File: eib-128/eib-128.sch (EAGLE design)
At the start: 46 parts

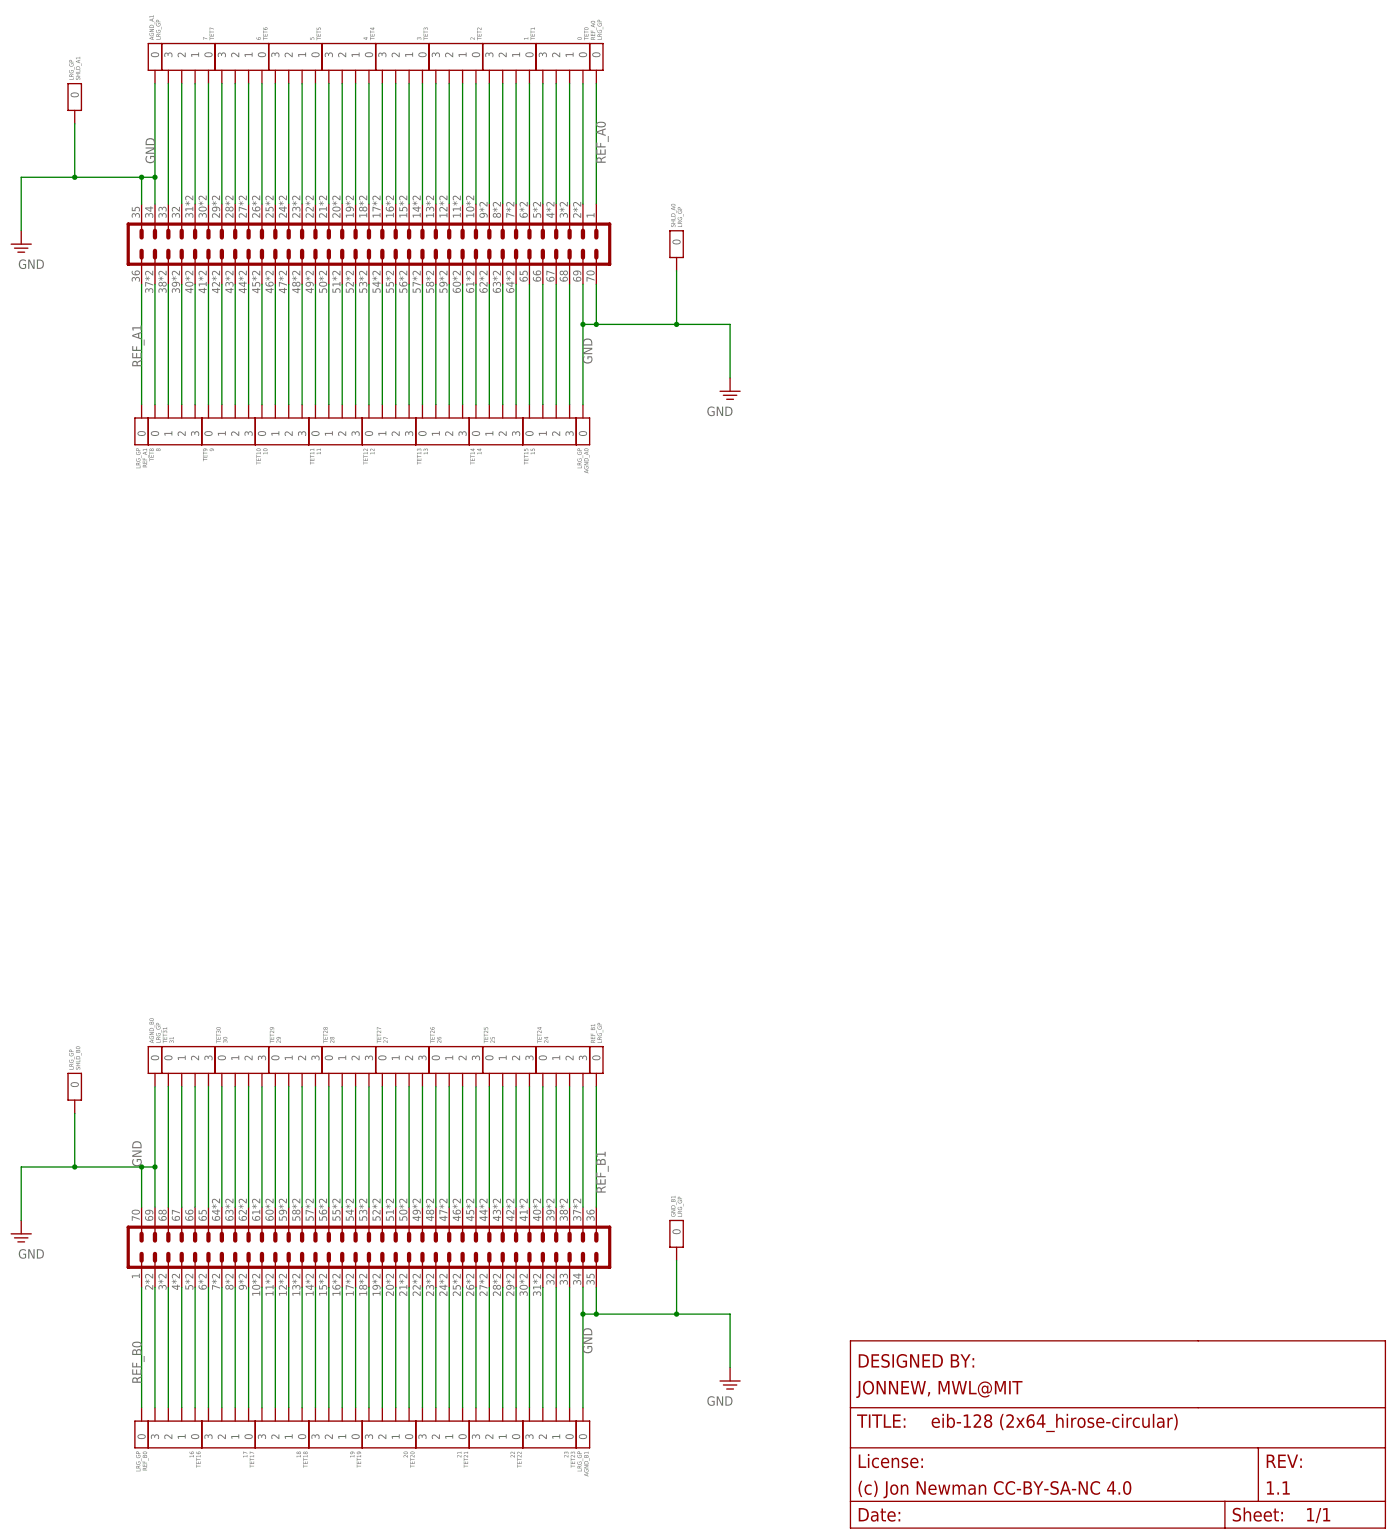
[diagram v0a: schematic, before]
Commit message: Updated eib-128 to match next-gen drive form factor.
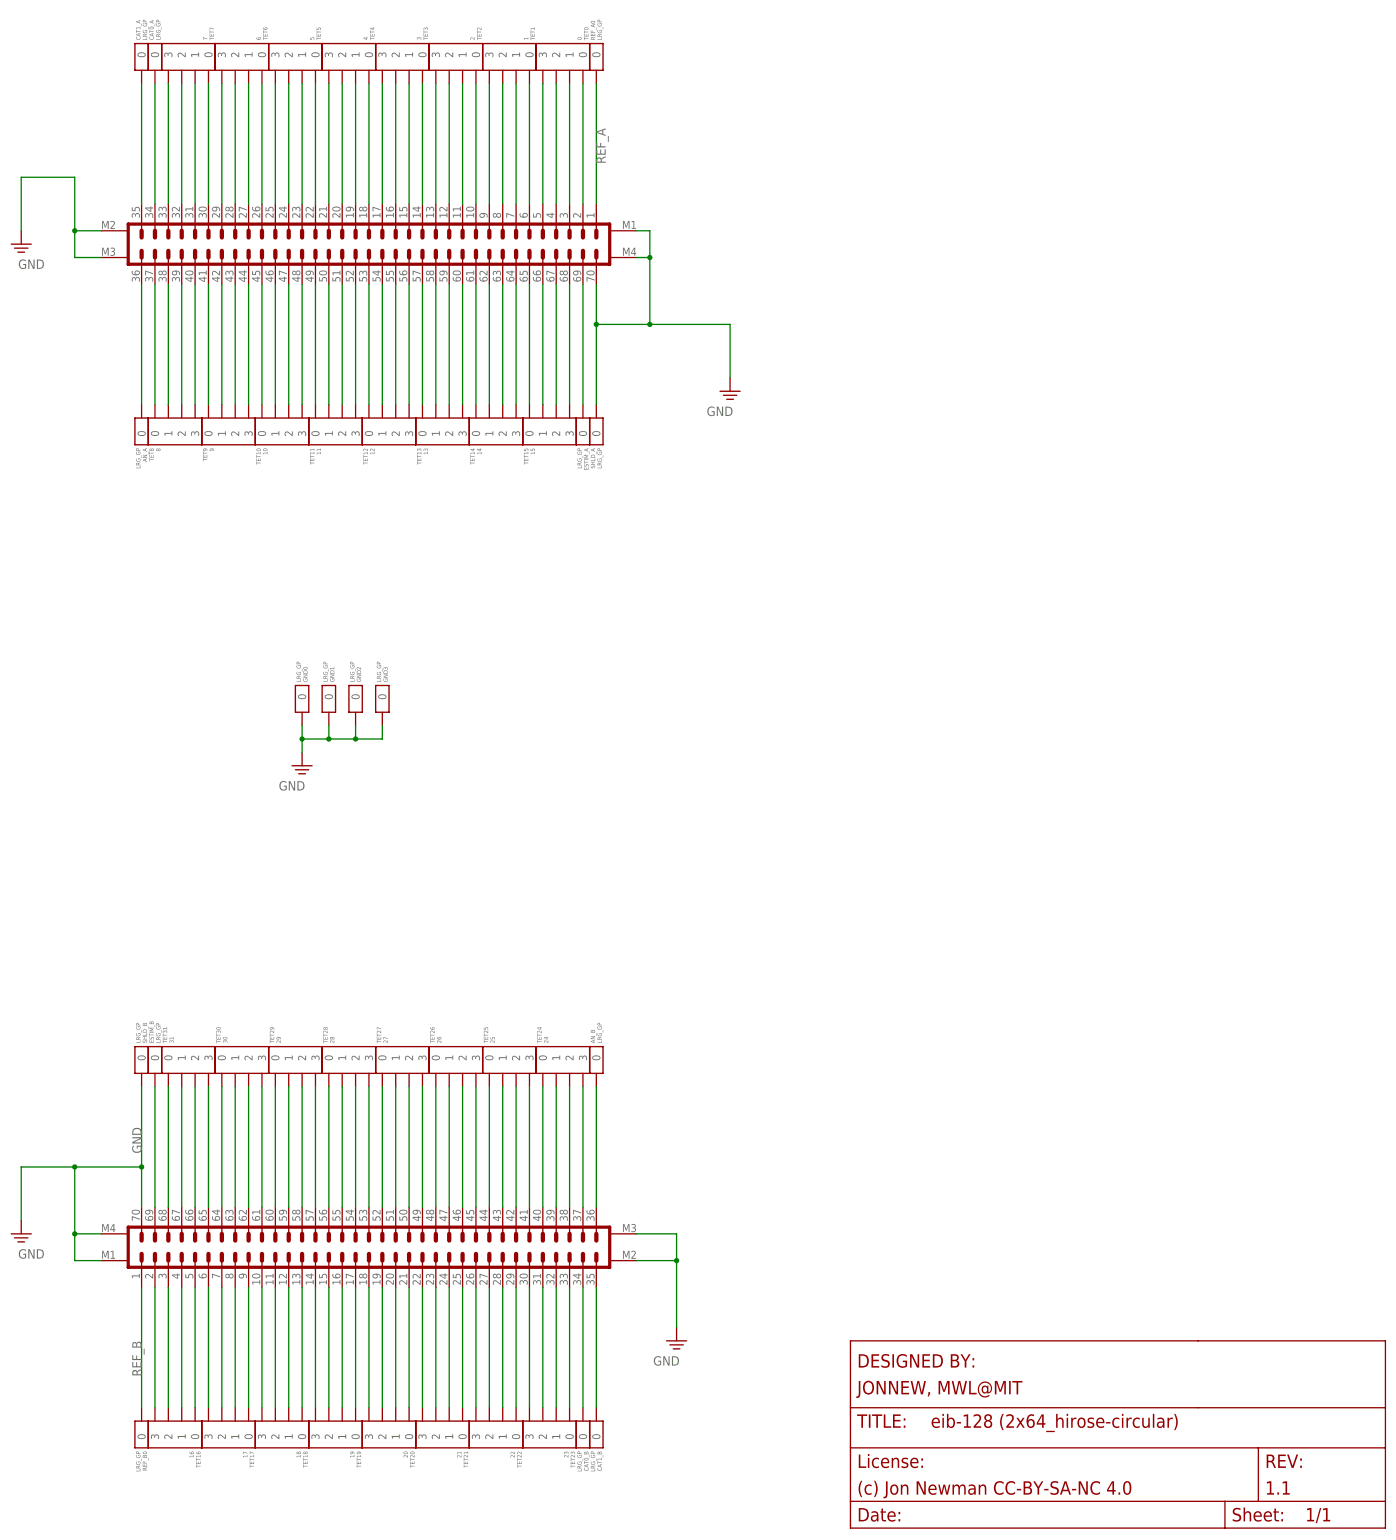
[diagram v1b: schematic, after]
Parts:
- removed AIN_N0T, AIN_S0T: DF40HEAD, jonnew:PINHD-2X35_DF40HEAD-EIB
- removed GND_B1, SHLD_A0, SHLD_A1, SHLD_B0: LRG_GP, jonnew:GOLDPIN_0.5ID_0.7OD
- added A, B: DF40HEAD, jonnew:PINHD-2X35+4_DF40-70HEAD
- added CAT1_A, CAT1_B, GND0, GND1, GND2, GND3, SHLD_A, SHLD_B: LRG_GP, jonnew:GOLDPIN_0.5ID_0.7OD
- renumbered AGND_A0 to ESTIM_A, AGND_A1 to CAT0_A, AGND_B0 to ESTIM_B, AGND_B1 to CAT0_B, REF_A1 to AN_A, REF_B1 to AN_B
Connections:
- removed net REF_A0: AIN_N0T.1, REF_A0.0
- removed net REF_A1: AIN_N0T.36, AN_A.0
- removed net REF_B0: AIN_S0T.1, REF_B0.0
- removed net REF_B1: AIN_S0T.36, AN_B.0
- new net AN_A: A.36, AN_A.0
- new net AN_B: AN_B.0, B.36
- new net CAT0_A: A.34, CAT0_A.0
- new net CAT0_B: B.34, CAT0_B.0
- new net CAT1_A: A.35, CAT1_A.0
- new net CAT1_B: B.35, CAT1_B.0
- new net ESTIM_A: A.69, ESTIM_A.0
- new net ESTIM_B: B.69, ESTIM_B.0
- new net REF_A: A.1, REF_A0.0
- new net REF_B: B.1, REF_B0.0
- net GND: now also A.70, A.M1, A.M2, A.M3, A.M4, B.70, B.M1, B.M2, B.M3, B.M4, GND0.0, GND1.0, GND2.0, GND3.0, SHLD_A.0, SHLD_B.0; no longer AIN_N0T.34, AIN_N0T.35, AIN_N0T.69, AIN_N0T.70, AIN_S0T.34, AIN_S0T.35, AIN_S0T.69, AIN_S0T.70, CAT0_A.0, CAT0_B.0, ESTIM_A.0, ESTIM_B.0, GND_B1.0, SHLD_A0.0, SHLD_A1.0, SHLD_B0.0
- net N$100: now also B.42; no longer AIN_S0T.42
- net N$1000: now also A.37; no longer AIN_N0T.37
- net N$101: now also B.43; no longer AIN_S0T.43
- net N$102: now also B.44; no longer AIN_S0T.44
- net N$103: now also B.45; no longer AIN_S0T.45
- net N$104: now also B.46; no longer AIN_S0T.46
- net N$105: now also B.47; no longer AIN_S0T.47
- net N$106: now also B.48; no longer AIN_S0T.48
- net N$107: now also B.49; no longer AIN_S0T.49
- net N$108: now also B.50; no longer AIN_S0T.50
- net N$109: now also B.51; no longer AIN_S0T.51
- net N$110: now also B.52; no longer AIN_S0T.52
- net N$111: now also B.53; no longer AIN_S0T.53
- net N$112: now also B.54; no longer AIN_S0T.54
- net N$113: now also B.55; no longer AIN_S0T.55
- net N$114: now also B.56; no longer AIN_S0T.56
- net N$115: now also B.57; no longer AIN_S0T.57
- net N$116: now also B.58; no longer AIN_S0T.58
- net N$117: now also B.59; no longer AIN_S0T.59
- net N$118: now also B.60; no longer AIN_S0T.60
- net N$119: now also B.61; no longer AIN_S0T.61
- net N$120: now also B.62; no longer AIN_S0T.62
- net N$121: now also B.63; no longer AIN_S0T.63
- net N$122: now also B.64; no longer AIN_S0T.64
- net N$123: now also B.65; no longer AIN_S0T.65
- net N$124: now also B.66; no longer AIN_S0T.66
- net N$125: now also B.67; no longer AIN_S0T.67
- net N$126: now also B.68; no longer AIN_S0T.68
- net N$127: now also B.2; no longer AIN_S0T.2
- net N$128: now also B.37; no longer AIN_S0T.37
- net N$199: now also A.33; no longer AIN_N0T.33
- net N$200: now also A.32; no longer AIN_N0T.32
- net N$201: now also A.31; no longer AIN_N0T.31
- net N$202: now also A.30; no longer AIN_N0T.30
- net N$203: now also A.29; no longer AIN_N0T.29
- net N$204: now also A.28; no longer AIN_N0T.28
- net N$205: now also A.27; no longer AIN_N0T.27
- net N$206: now also A.26; no longer AIN_N0T.26
- net N$207: now also A.25; no longer AIN_N0T.25
- net N$208: now also A.24; no longer AIN_N0T.24
- net N$209: now also A.23; no longer AIN_N0T.23
- net N$210: now also A.22; no longer AIN_N0T.22
- net N$211: now also A.21; no longer AIN_N0T.21
- net N$212: now also A.20; no longer AIN_N0T.20
- net N$213: now also A.19; no longer AIN_N0T.19
- net N$214: now also A.18; no longer AIN_N0T.18
- net N$215: now also A.17; no longer AIN_N0T.17
- net N$216: now also A.16; no longer AIN_N0T.16
- net N$217: now also A.15; no longer AIN_N0T.15
- net N$218: now also A.14; no longer AIN_N0T.14
- net N$219: now also A.13; no longer AIN_N0T.13
- net N$220: now also A.12; no longer AIN_N0T.12
- net N$221: now also A.11; no longer AIN_N0T.11
- net N$222: now also A.10; no longer AIN_N0T.10
- net N$223: now also A.9; no longer AIN_N0T.9
- net N$224: now also A.8; no longer AIN_N0T.8
- net N$225: now also A.7; no longer AIN_N0T.7
- net N$226: now also A.6; no longer AIN_N0T.6
- net N$227: now also A.5; no longer AIN_N0T.5
- net N$228: now also A.4; no longer AIN_N0T.4
- net N$229: now also A.3; no longer AIN_N0T.3
- net N$230: now also A.2; no longer AIN_N0T.2
- net N$231: now also A.38; no longer AIN_N0T.38
- net N$232: now also A.39; no longer AIN_N0T.39
- net N$233: now also A.40; no longer AIN_N0T.40
- net N$234: now also A.41; no longer AIN_N0T.41
- net N$235: now also A.42; no longer AIN_N0T.42
- net N$236: now also A.43; no longer AIN_N0T.43
- net N$237: now also A.44; no longer AIN_N0T.44
- net N$238: now also A.45; no longer AIN_N0T.45
- net N$239: now also A.46; no longer AIN_N0T.46
- net N$240: now also A.47; no longer AIN_N0T.47
- net N$241: now also A.48; no longer AIN_N0T.48
- net N$242: now also A.49; no longer AIN_N0T.49
- net N$243: now also A.50; no longer AIN_N0T.50
- net N$244: now also A.51; no longer AIN_N0T.51
- net N$245: now also A.52; no longer AIN_N0T.52
- net N$246: now also A.53; no longer AIN_N0T.53
- net N$247: now also A.54; no longer AIN_N0T.54
- net N$248: now also A.55; no longer AIN_N0T.55
- net N$249: now also A.56; no longer AIN_N0T.56
- net N$250: now also A.57; no longer AIN_N0T.57
- net N$251: now also A.58; no longer AIN_N0T.58
- net N$252: now also A.59; no longer AIN_N0T.59
- net N$253: now also A.60; no longer AIN_N0T.60
- net N$254: now also A.61; no longer AIN_N0T.61
- net N$255: now also A.62; no longer AIN_N0T.62
- net N$256: now also A.63; no longer AIN_N0T.63
- net N$257: now also A.64; no longer AIN_N0T.64
- net N$258: now also A.65; no longer AIN_N0T.65
- net N$259: now also A.66; no longer AIN_N0T.66
- net N$260: now also A.67; no longer AIN_N0T.67
- net N$261: now also A.68; no longer AIN_N0T.68
- net N$65: now also B.33; no longer AIN_S0T.33
- net N$66: now also B.32; no longer AIN_S0T.32
- net N$67: now also B.31; no longer AIN_S0T.31
- net N$68: now also B.30; no longer AIN_S0T.30
- net N$69: now also B.29; no longer AIN_S0T.29
- net N$70: now also B.28; no longer AIN_S0T.28
- net N$71: now also B.27; no longer AIN_S0T.27
- net N$72: now also B.26; no longer AIN_S0T.26
- net N$73: now also B.25; no longer AIN_S0T.25
- net N$74: now also B.24; no longer AIN_S0T.24
- net N$75: now also B.23; no longer AIN_S0T.23
- net N$76: now also B.22; no longer AIN_S0T.22
- net N$77: now also B.21; no longer AIN_S0T.21
- net N$78: now also B.20; no longer AIN_S0T.20
- net N$79: now also B.19; no longer AIN_S0T.19
- net N$80: now also B.18; no longer AIN_S0T.18
- net N$81: now also B.17; no longer AIN_S0T.17
- net N$82: now also B.16; no longer AIN_S0T.16
- net N$83: now also B.15; no longer AIN_S0T.15
- net N$84: now also B.14; no longer AIN_S0T.14
- net N$85: now also B.13; no longer AIN_S0T.13
- net N$86: now also B.12; no longer AIN_S0T.12
- net N$87: now also B.11; no longer AIN_S0T.11
- net N$88: now also B.10; no longer AIN_S0T.10
- net N$89: now also B.9; no longer AIN_S0T.9
- net N$90: now also B.8; no longer AIN_S0T.8
- net N$91: now also B.7; no longer AIN_S0T.7
- net N$92: now also B.6; no longer AIN_S0T.6
- net N$93: now also B.5; no longer AIN_S0T.5
- net N$94: now also B.4; no longer AIN_S0T.4
- net N$95: now also B.3; no longer AIN_S0T.3
- net N$96: now also B.38; no longer AIN_S0T.38
- net N$97: now also B.39; no longer AIN_S0T.39
- net N$98: now also B.40; no longer AIN_S0T.40
- net N$99: now also B.41; no longer AIN_S0T.41
